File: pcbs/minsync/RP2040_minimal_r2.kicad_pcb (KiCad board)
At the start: 2 copper layers, 42 x 42 mm, 35 parts, among them J1 SWD_CONN, J2 Comm, J4 Comm, J5 Comm, J6 Comm, U1 NCP1117-3.3_SOT223, U2 W25Q128JVS, U3 RP2040, U4 Si5351A-B-GT, Y2 Crystal_GND24

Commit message: Route most of the minsync PCB
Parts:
- moved H3 98.5 mm to (117.0, 117.0)
- moved H4 96.2 mm to (83.0, 117.0)
- moved H1 62.2 mm to (117.0, 83.0)
- moved H2 51.0 mm to (83.0, 83.0)
- moved J4 24.6 mm to (84.0, 105.1), turned to 180 degrees
- moved J2 24.2 mm to (94.9, 84.0), turned to 90 degrees
- moved J1 9.30 mm to (113.8, 110.0), turned to -45 degrees
- moved R1 3.87 mm to (89.0, 86.5)
- moved R2 3.87 mm to (87.5, 86.5)
- moved C5 3.87 mm to (94.1, 87.0)
- moved U2 3.61 mm to (91.0, 91.0)
- moved C17 2.66 mm to (98.0, 87.0)
- moved C4 1.99 mm to (118.2, 89.8), turned to -90 degrees
- moved C11 1.56 mm to (95.0, 96.5), turned to 90 degrees
- moved J5 1.00 mm to (105.1, 116.0)
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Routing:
- net VBUS: track 0.00 -> 89.0 mm
- net /GPIO2: track 0.00 -> 33.7 mm, vias 0 -> 1
- net /GPIO0: track 0.00 -> 32.3 mm, vias 0 -> 1
- net /GPIO1: track 0.00 -> 30.3 mm, vias 0 -> 1
- net /GPIO3: track 0.00 -> 27.2 mm, vias 0 -> 1
- net /GPIO4: track 0.00 -> 26.4 mm, vias 0 -> 1
- net /GPIO5: track 0.00 -> 25.4 mm, vias 0 -> 1
- net /GPIO14: track 0.00 -> 21.0 mm
- net /GPIO12: track 0.00 -> 20.6 mm
- net /GPIO7: track 0.00 -> 19.9 mm
- net /GPIO20: track 0.00 -> 18.8 mm
- net /GPIO13: track 0.00 -> 18.8 mm
- net /GPIO8: track 0.00 -> 18.5 mm
- net /QSPI_SS: track 4.09 -> 22.5 mm
- net /GPIO19: track 0.00 -> 18.4 mm, vias 0 -> 1
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- added copper zone on B.Cu, net GND
- added copper zone on F.Cu, net GND
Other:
- outline, holes or cut-outs redrawn

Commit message: Update minsync PCB
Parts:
- removed TP2, TP3, TP4: TestPoint, TestPoint:TestPoint_Keystone_5019_Minature
- added D1: LED, LED_SMD:LED_0603_1608Metric, F.Cu at (119.2, 89.2)
- added D2: LED, LED_SMD:LED_0603_1608Metric, F.Cu at (117.6, 89.2)
- added J3: Conn_01x01_Pin, Connector_PinHeader_1.27mm:PinHeader_1x01_P1.27mm_Vertical, F.Cu at (112.1, 101.5)
- added R3: 470R, Resistor_SMD:R_0402_1005Metric, F.Cu at (109.0, 96.9)
- added R4: 470R, Resistor_SMD:R_0402_1005Metric, F.Cu at (105.2, 97.0)
- added SW1: SW_Push, Button_Switch_SMD:SW_Push_SPST_NO_Alps_SKRK, F.Cu at (83.0, 89.1)
- TP1: footprint TestPoint:TestPoint_Keystone_5019_Minature -> Connector_PinHeader_2.54mm:PinHeader_1x01_P2.54mm_Vertical
- moved TP1 31.6 mm to (112.3, 97.6)
- moved C1 7.99 mm to (110.2, 82.4), turned to 0 degrees
- moved C4 7.86 mm to (111.4, 93.6), turned to 0 degrees
- moved C16 5.79 mm to (104.8, 89.1), turned to 90 degrees
- moved R2 2.29 mm to (89.5, 87.5), turned to 180 degrees
- moved C10 1.77 mm to (102.9, 94.9)
- moved C8 1.77 mm to (101.9, 94.9)
- moved U1 1.54 mm to (110.5, 88.0), turned to -90 degrees
- moved R1 1.45 mm to (87.5, 86.5)
- moved C15 0.73 mm to (105.8, 95.7)
- moved C6 0.60 mm to (99.6, 92.5)
- moved C9 0.60 mm to (100.6, 92.5)
- moved C11 0.58 mm to (95.2, 96.0)
- moved C13 0.10 mm to (93.6, 101.2)
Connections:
- TP1 pad 1: /SI_CLK0 -> /GPIO25
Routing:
- net VBUS: track 89.0 -> 130.2 mm
- net /GPIO27_ADC1: track 0.00 -> 31.4 mm, vias 0 -> 2
- net /GPIO26_ADC0: track 0.00 -> 29.9 mm, vias 0 -> 2
- net Net-(D2-A): track 0.00 -> 15.0 mm
- net /RUN: track 0.00 -> 14.5 mm, vias 0 -> 1
- net Net-(D1-A): track 0.00 -> 12.6 mm
- net /GPIO25: track 0.00 -> 9.61 mm
- net GND: track 21.4 -> 28.6 mm, vias 18 -> 22
- net +3V3: track 26.5 -> 19.5 mm
- net /GPIO28_ADC2: track 0.00 -> 5.58 mm
- net /~{USB_BOOT}: track 0.00 -> 4.92 mm
- net /GPIO8: track 18.5 -> 21.5 mm, vias 0 -> 1
- net +1V1: track 17.0 -> 14.4 mm
- net /GPIO12: track 20.6 -> 22.8 mm
- net /GPIO29_ADC3: track 0.00 -> 1.59 mm
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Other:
- board text added: "minsync v0.1"
- board text removed: "USB_BOOT"

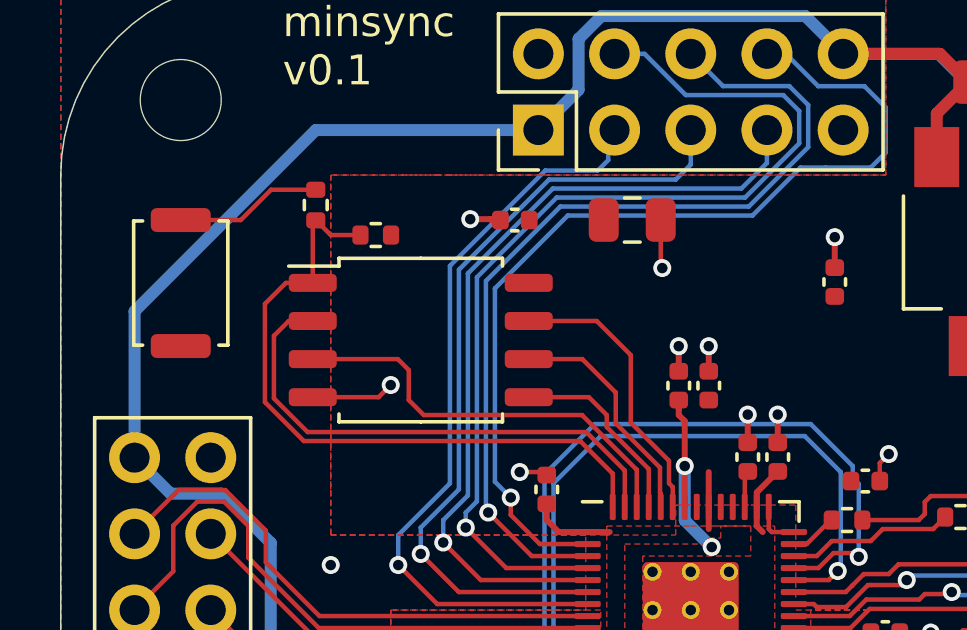
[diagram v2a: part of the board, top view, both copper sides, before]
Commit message: Add BOM and CPL of minsync v0.1
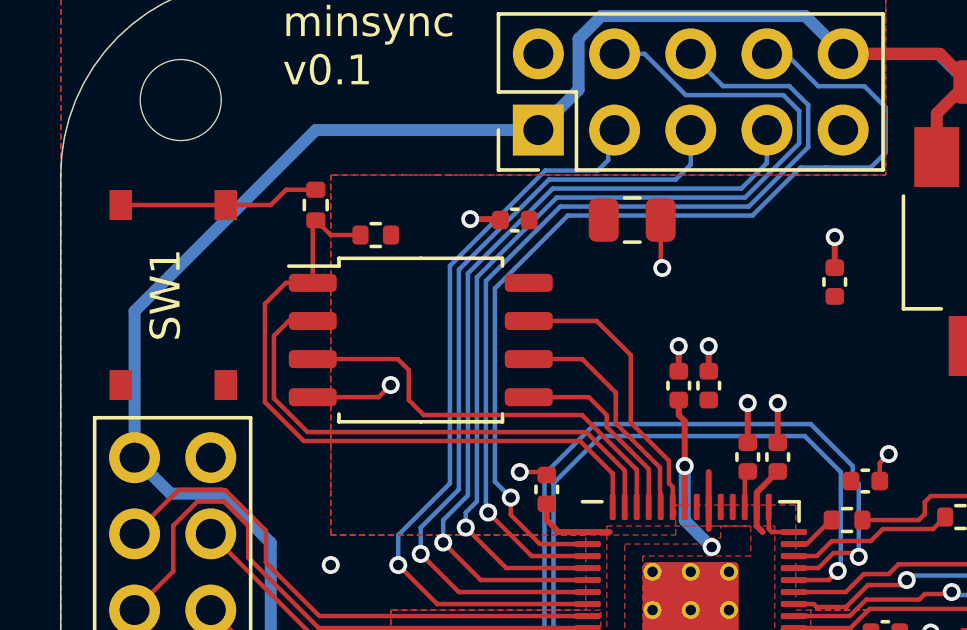
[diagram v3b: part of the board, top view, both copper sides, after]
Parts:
- SW1: footprint Button_Switch_SMD:SW_Push_SPST_NO_Alps_SKRK -> RP2040_minimal:TS-1187A-PushButton
- moved SW1 0.40 mm to (83.0, 89.5)
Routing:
- net /~{USB_BOOT}: track 4.92 -> 6.71 mm
- net GND: track 28.6 -> 29.3 mm

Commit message: Clock experiments
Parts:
- added J8: SSD1306, Connector_PinHeader_2.54mm:PinHeader_1x04_P2.54mm_Vertical, B.Cu at (83.6, 110.8)
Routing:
- net /GPIO28_ADC2: track 5.58 -> 50.2 mm, vias 0 -> 1
- net /GPIO29_ADC3: track 1.59 -> 42.4 mm, vias 0 -> 1
- net +3V3: track 19.5 -> 31.3 mm, vias 0 -> 1
- net /GPIO4: track 26.4 -> 28.3 mm
- net /GPIO5: track 25.4 -> 26.8 mm
- net VBUS: track 130.2 -> 128.7 mm
- net /GPIO1: track 30.3 -> 31.7 mm
- net /GPIO3: track 27.2 -> 28.6 mm
- net /GPIO2: track 33.7 -> 35.1 mm
- net /GPIO0: track 31.8 -> 32.5 mm
- net GND: vias 22 -> 23

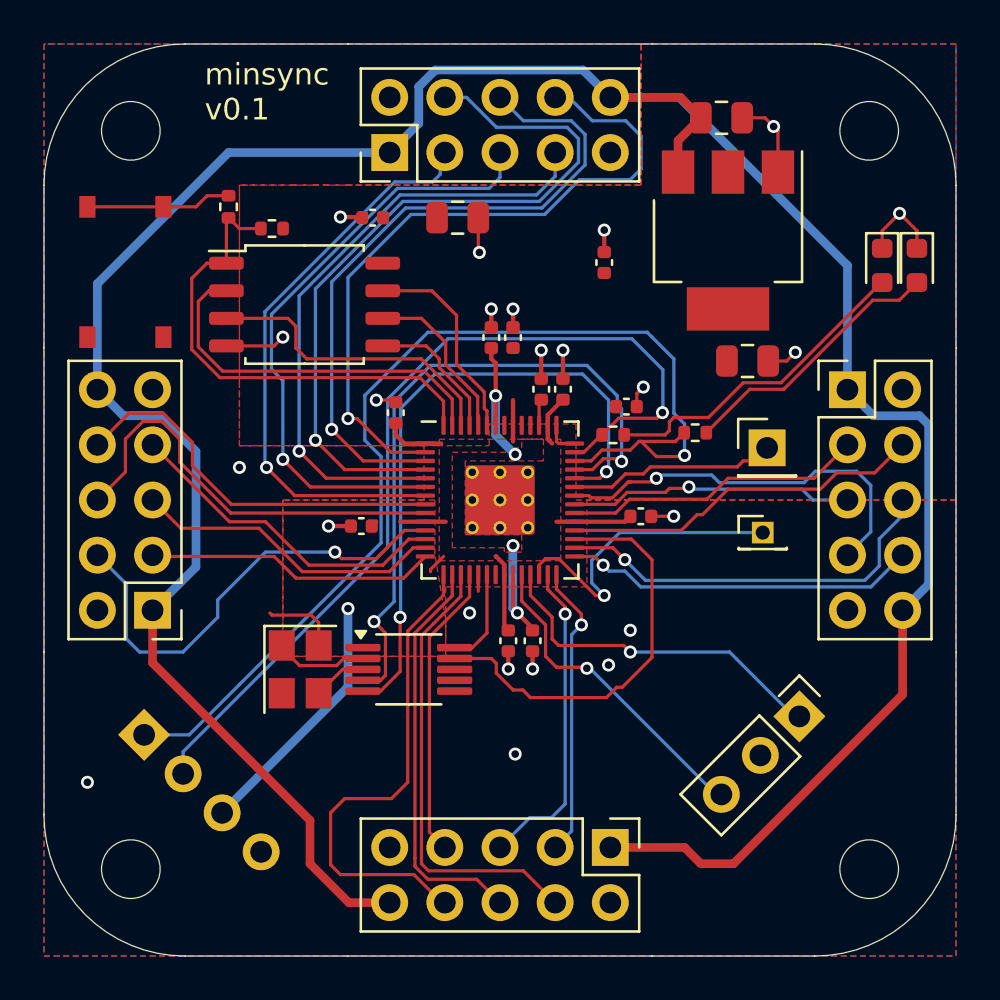
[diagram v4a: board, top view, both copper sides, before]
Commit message: Switch to 2x4P headers
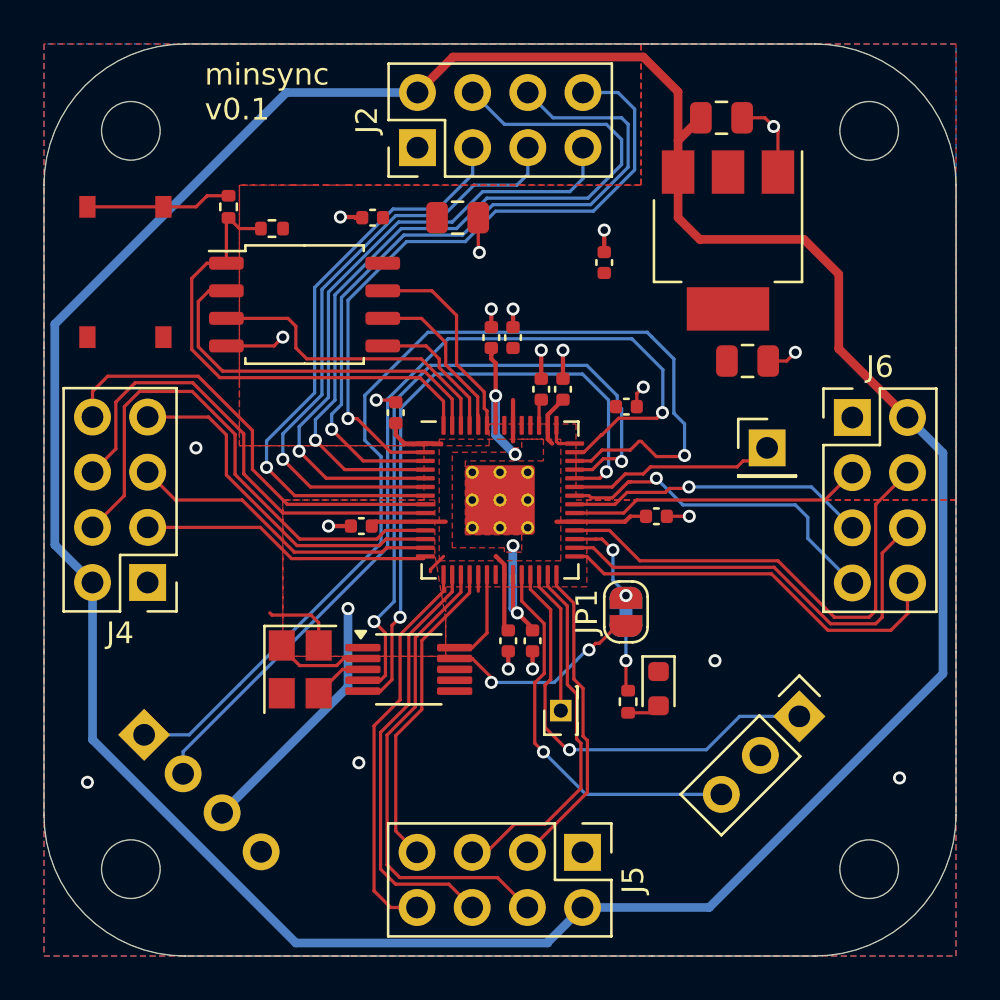
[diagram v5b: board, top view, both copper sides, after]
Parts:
- removed D2: LED, LED_SMD:LED_0603_1608Metric
- removed R4: 470R, Resistor_SMD:R_0402_1005Metric
- added JP1: GPIN_to_Si, Jumper:SolderJumper-2_P1.3mm_Open_RoundedPad1.0x1.5mm, F.Cu at (105.8, 105.2)
- added JP2: GPIN_to_LED, Jumper:SolderJumper-2_P1.3mm_Bridged_RoundedPad1.0x1.5mm, B.Cu at (105.8, 105.2)
- J2, J4, J5, J6: footprint Connector_PinHeader_2.54mm:PinHeader_2x05_P2.54mm_Vertical -> Connector_PinHeader_2.54mm:PinHeader_2x04_P2.54mm_Vertical
- moved D1 22.8 mm to (107.3, 108.7)
- moved R3 12.8 mm to (105.9, 109.3), turned to 90 degrees
- moved J3 12.4 mm to (102.8, 109.7), turned to 90 degrees
- moved J2 1.30 mm to (96.2, 83.8)
- moved J4 1.30 mm to (83.8, 103.8)
- moved J5 1.30 mm to (103.8, 116.2)
- moved J6 1.30 mm to (116.2, 96.2)
- moved C12 0.72 mm to (107.2, 100.8)
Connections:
- J2 pad 1: VBUS -> GND
- J2 pad 2: GND -> VBUS
- J4 pad 1: VBUS -> GND
- J4 pad 2: GND -> VBUS
- J5 pad 1: VBUS -> GND
- J5 pad 2: GND -> VBUS
- J6 pad 1: VBUS -> GND
- J6 pad 2: GND -> VBUS
- R3 pad 2: /GPIO28_ADC2 -> Net-(JP2-A)
- U4 pad 9: /GPIO20 -> /SI_CLK1
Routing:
- net Net-(D2-A): track 15.0 -> 0.00 mm
- net /GPIO20: track 19.3 -> 4.42 mm, vias 0 -> 2
- net Net-(D1-A): track 12.6 -> 1.53 mm
- net VBUS: track 128.7 -> 138.7 mm
- net /SI_CLK1: track 0.00 -> 9.43 mm, vias 0 -> 2
- net /RUN: track 14.5 -> 6.68 mm, vias 1 -> 0
- net /GPIO21: track 16.7 -> 22.6 mm
- net /GPIO12: track 22.8 -> 18.2 mm
- net /SWD: track 16.3 -> 20.3 mm
- net GND: track 29.3 -> 25.4 mm, vias 23 -> 21
- net Net-(JP2-A): track 0.00 -> 3.02 mm, vias 0 -> 1
- net /GPIO8: track 21.5 -> 24.4 mm, vias 1 -> 0
- net /SWCLK: track 15.0 -> 18.0 mm
- net /GPIO24: track 18.4 -> 15.8 mm
- net /GPIO1: track 31.7 -> 34.2 mm
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
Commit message: Use 2x4P headers for connectors
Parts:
- renumbered J2 to J1, J4 to J2, J5 to J3, J6 to J4, J1 to J5, J3 to J6, J8 to J7

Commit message: Implement minsync_connect v0.1
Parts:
- J1, J2, J3, J4: footprint Connector_PinHeader_2.54mm:PinHeader_2x04_P2.54mm_Vertical -> RP2040_minimal:pitopi_and_power
- moved J1 4.01 mm to (100.0, 82.5), turned to -90 degrees
- moved J2 4.01 mm to (82.5, 100.0), turned to 0 degrees
- moved J3 4.01 mm to (100.0, 117.5), turned to 90 degrees
- moved J4 4.01 mm to (117.5, 100.0), turned to 180 degrees

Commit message: Dry run ordering minsync and minsync connect v0.1
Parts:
- moved TP1 10.1 mm to (119.0, 90.0)
- moved J7 2.12 mm to (85.1, 109.3)
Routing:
- net /GPIO25: track 9.61 -> 20.6 mm, vias 0 -> 1
- net /GPIO28_ADC2: track 48.0 -> 45.9 mm
- net +3V3: track 33.1 -> 31.0 mm
- net /GPIO29_ADC3: track 42.4 -> 40.3 mm
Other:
- board text added: "E"
- board text added: "N"
- board text added: "S"
- board text added: "W"
